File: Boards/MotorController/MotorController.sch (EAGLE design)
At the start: 16 parts, among them IC1 MC33926

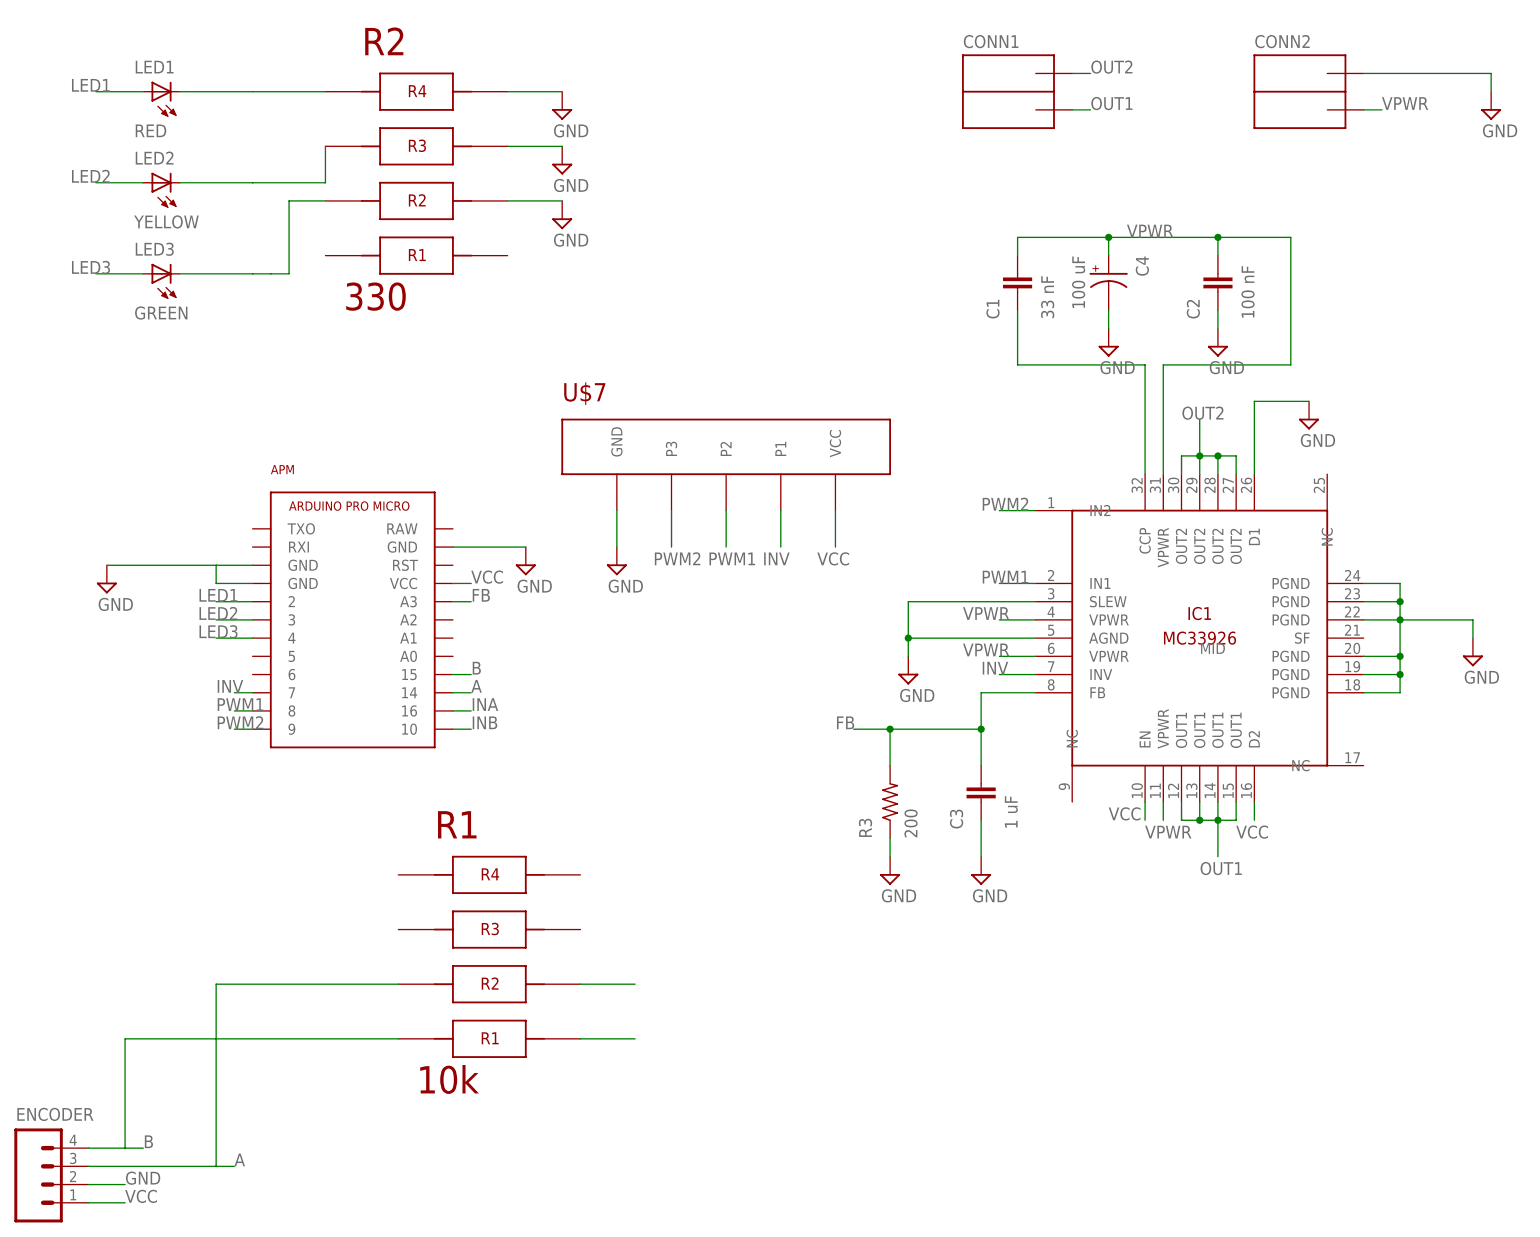
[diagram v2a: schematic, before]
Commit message: Fixed routing to arduino pins
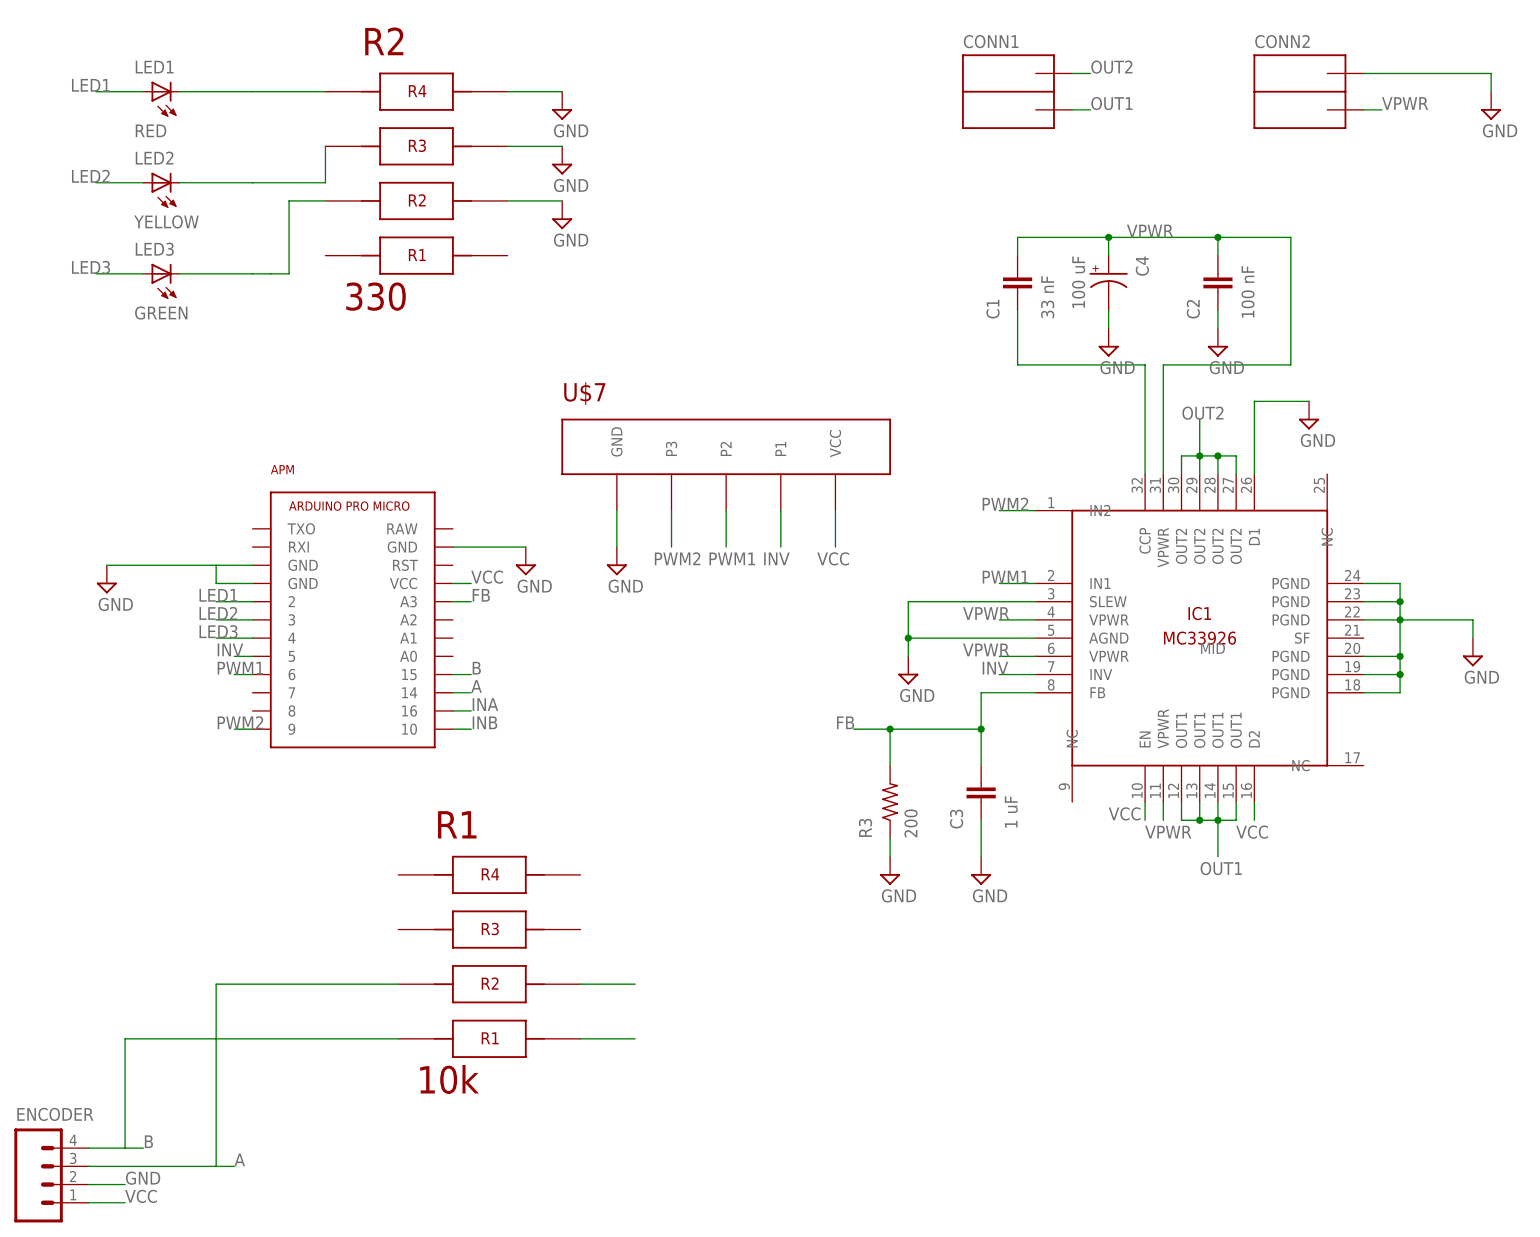
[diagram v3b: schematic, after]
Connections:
- net INV: now also APM.5; no longer APM.7
- net PWM1: now also APM.6; no longer APM.8
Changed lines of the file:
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@@
 <?xml version="1.0" encoding="utf-8"?>
 <!DOCTYPE eagle SYSTEM "eagle.dtd">
-<eagle version="9.1.3">
+<eagle version="9.2.0">
 <drawing>
 <settings>
@@
 </plain>
 <instances>
-<instance part="APM" gate="APM" x="60.96" y="93.98"/>
+<instance part="APM" gate="APM" x="60.96" y="93.98">
+<attribute name="NAME" x="50.8" y="114.3" size="1.27" layer="94"/>
+</instance>
 <instance part="FRAME1" gate="G$1" x="0" y="0">
 <attribute name="AUTHOR" x="0" y="0" size="1.778" layer="96" display="off"/>
 </instance>
 <instance part="FRAME1" gate="G$2" x="147.32" y="0">
-<attribute name="REVISION" x="147.32" y="0" size="1.778" layer="96"/>
-</instance>
-<instance part="SUPPLY2" gate="GND" x="27.94" y="99.06"/>
-<instance part="SUPPLY3" gate="GND" x="86.36" y="101.6"/>
-<instance part="LED1" gate="G$1" x="35.56" y="167.64"/>
-<instance part="SUPPLY4" gate="GND" x="91.44" y="165.1"/>
-<instance part="LED2" gate="G$1" x="35.56" y="154.94"/>
-<instance part="SUPPLY5" gate="GND" x="91.44" y="157.48"/>
-<instance part="LED3" gate="G$1" x="35.56" y="142.24"/>
-<instance part="SUPPLY6" gate="GND" x="91.44" y="149.86"/>
-<instance part="ENCODER" gate="G$1" x="17.78" y="17.78"/>
-<instance part="R1" gate="G$1" x="81.28" y="33.02"/>
-<instance part="R2" gate="G$1" x="71.12" y="142.24"/>
-<instance part="IC1" gate="G$1" x="180.34" y="91.44"/>
-<instance part="SUPPLY1" gate="GND" x="218.44" y="88.9"/>
-<instance part="SUPPLY7" gate="GND" x="195.58" y="121.92"/>
-<instance part="SUPPLY8" gate="GND" x="139.7" y="86.36"/>
-<instance part="C1" gate="G$1" x="154.94" y="139.7" rot="R90"/>
-<instance part="C2" gate="G$1" x="182.88" y="139.7" rot="R90"/>
-<instance part="C3" gate="G$1" x="149.86" y="68.58" rot="R90"/>
-<instance part="SUPPLY9" gate="GND" x="182.88" y="132.08"/>
-<instance part="SUPPLY10" gate="GND" x="167.64" y="132.08"/>
-<instance part="SUPPLY11" gate="GND" x="149.86" y="58.42"/>
-<instance part="SUPPLY12" gate="GND" x="137.16" y="58.42"/>
-<instance part="C4" gate="G$1" x="167.64" y="142.24" rot="R270"/>
-<instance part="R3" gate="G$1" x="137.16" y="68.58" rot="R90"/>
-<instance part="CONN1" gate="G$1" x="154.94" y="167.64"/>
-<instance part="CONN2" gate="G$1" x="195.58" y="167.64"/>
-<instance part="SUPPLY14" gate="GND" x="220.98" y="165.1"/>
-<instance part="U$7" gate="G$1" x="91.44" y="114.3"/>
-<instance part="SUPPLY13" gate="GND" x="99.06" y="101.6"/>
+<attribute name="LAST_DATE_TIME" x="160.02" y="1.27" size="2.54" layer="94" font="vector"/>
+<attribute name="SHEET" x="233.68" y="1.27" size="2.54" layer="94" font="vector"/>
+<attribute name="DRAWING_NAME" x="162.814" y="17.78" size="2.7432" layer="94" font="vector"/>
+<attribute name="AUTHOR" x="148.59" y="6.985" size="2.7432" layer="94" font="vector"/>
+<attribute name="REVISION" x="236.22" y="6.985" size="2.7432" layer="94" font="vector"/>
+</instance>
+<instance part="SUPPLY2" gate="GND" x="27.94" y="99.06">
+<attribute name="VALUE" x="26.67" y="95.25" size="1.778" layer="96"/>
+</instance>
+<instance part="SUPPLY3" gate="GND" x="86.36" y="101.6">
+<attribute name="VALUE" x="85.09" y="97.79" size="1.778" layer="96"/>
+</instance>
+<instance part="LED1" gate="G$1" x="35.56" y="167.64">
+<attribute name="NAME" x="31.75" y="170.18" size="1.778" layer="95"/>
+<attribute name="VALUE" x="31.75" y="161.29" size="1.778" layer="96"/>
+</instance>
+<instance part="SUPPLY4" gate="GND" x="91.44" y="165.1">
+<attribute name="VALUE" x="90.17" y="161.29" size="1.778" layer="96"/>
+</instance>
+<instance part="LED2" gate="G$1" x="35.56" y="154.94">
+<attribute name="NAME" x="31.75" y="157.48" size="1.778" layer="95"/>
+<attribute name="VALUE" x="31.75" y="148.59" size="1.778" layer="96"/>
+</instance>
+<instance part="SUPPLY5" gate="GND" x="91.44" y="157.48">
+<attribute name="VALUE" x="90.17" y="153.67" size="1.778" layer="96"/>
+</instance>
+<instance part="LED3" gate="G$1" x="35.56" y="142.24">
+<attribute name="NAME" x="31.75" y="144.78" size="1.778" layer="95"/>
+<attribute name="VALUE" x="31.75" y="135.89" size="1.778" layer="96"/>
+</instance>
+<instance part="SUPPLY6" gate="GND" x="91.44" y="149.86">
+<attribute name="VALUE" x="90.17" y="146.05" size="1.778" layer="96"/>
+</instance>
+<instance part="ENCODER" gate="G$1" x="17.78" y="17.78">
+<attribute name="VALUE" x="15.24" y="7.62" size="1.778" layer="96"/>
+<attribute name="NAME" x="15.24" y="24.13" size="1.778" layer="95"/>
+</instance>
+<instance part="R1" gate="G$1" x="81.28" y="33.02">
+<attribute name="NAME" x="73.66" y="63.5" size="3.81" layer="94" font="vector"/>
+<attribute name="VALUE" x="71.12" y="27.94" size="3.81" layer="94" font="vector"/>
+</instance>
+<instance part="R2" gate="G$1" x="71.12" y="142.24">
+<attribute name="NAME" x="63.5" y="172.72" size="3.81" layer="94" font="vector"/>
+<attribute name="VALUE" x="60.96" y="137.16" size="3.81" layer="94" font="vector"/>
+</instance>
+<instance part="IC1" gate="G$1" x="180.34" y="91.44">
+<attribute name="NAME" x="180.34" y="93.98" size="1.778" layer="94" align="bottom-center"/>
+</instance>
+<instance part="SUPPLY1" gate="GND" x="218.44" y="88.9">
+<attribute name="VALUE" x="217.17" y="85.09" size="1.778" layer="96"/>
+</instance>
+<instance part="SUPPLY7" gate="GND" x="195.58" y="121.92">
+<attribute name="VALUE" x="194.31" y="118.11" size="1.778" layer="96"/>
+</instance>
+<instance part="SUPPLY8" gate="GND" x="139.7" y="86.36">
+<attribute name="VALUE" x="138.43" y="82.55" size="1.778" layer="96"/>
+</instance>
+<instance part="C1" gate="G$1" x="154.94" y="139.7" rot="R90">
+<attribute name="NAME" x="152.4" y="135.89" size="1.778" layer="95" rot="R90"/>
+<attribute name="VALUE" x="160.02" y="135.89" size="1.778" layer="96" rot="R90"/>
+</instance>
+<instance part="C2" gate="G$1" x="182.88" y="139.7" rot="R90">
+<attribute name="NAME" x="180.34" y="135.89" size="1.778" layer="95" rot="R90"/>
+<attribute name="VALUE" x="187.96" y="135.89" size="1.778" layer="96" rot="R90"/>
+</instance>
+<instance part="C3" gate="G$1" x="149.86" y="68.58" rot="R90">
+<attribute name="NAME" x="147.32" y="64.77" size="1.778" layer="95" rot="R90"/>
+<attribute name="VALUE" x="154.94" y="64.77" size="1.778" layer="96" rot="R90"/>
+</instance>
+<instance part="SUPPLY9" gate="GND" x="182.88" y="132.08">
+<attribute name="VALUE" x="181.61" y="128.27" size="1.778" layer="96"/>
+</instance>
+<instance part="SUPPLY10" gate="GND" x="167.64" y="132.08">
+<attribute name="VALUE" x="166.37" y="128.27" size="1.778" layer="96"/>
+</instance>
+<instance part="SUPPLY11" gate="GND" x="149.86" y="58.42">
+<attribute name="VALUE" x="148.59" y="54.61" size="1.778" layer="96"/>
+</instance>
+<instance part="SUPPLY12" gate="GND" x="137.16" y="58.42">
+<attribute name="VALUE" x="135.89" y="54.61" size="1.778" layer="96"/>
+</instance>
+<instance part="C4" gate="G$1" x="167.64" y="142.24" rot="R270">
+<attribute name="NAME" x="171.45" y="144.78" size="1.778" layer="95" rot="R270"/>
+<attribute name="VALUE" x="162.56" y="144.78" size="1.778" layer="96" rot="R270"/>
+</instance>
+<instance part="R3" gate="G$1" x="137.16" y="68.58" rot="R90">
+<attribute name="NAME" x="134.62" y="63.5" size="1.778" layer="95" rot="R90"/>
+<attribute name="VALUE" x="140.97" y="63.5" size="1.778" layer="96" rot="R90"/>
+</instance>
+<instance part="CONN1" gate="G$1" x="154.94" y="167.64">
+<attribute name="NAME" x="147.32" y="173.736" size="1.778" layer="95"/>
+</instance>
+<instance part="CONN2" gate="G$1" x="195.58" y="167.64">
+<attribute name="NAME" x="187.96" y="173.736" size="1.778" layer="95"/>
+</instance>
+<instance part="SUPPLY14" gate="GND" x="220.98" y="165.1">
+<attribute name="VALUE" x="219.71" y="161.29" size="1.778" layer="96"/>
+</instance>
+<instance part="U$7" gate="G$1" x="91.44" y="114.3">
+<attribute name="NAME" x="91.44" y="124.46" size="2.54" layer="94" font="vector"/>
+</instance>
+<instance part="SUPPLY13" gate="GND" x="99.06" y="101.6">
+<attribute name="VALUE" x="97.79" y="97.79" size="1.778" layer="96"/>
+</instance>
 </instances>
 <busses>
@@
 </segment>
 <segment>
-<pinref part="APM" gate="APM" pin="7"/>
-<wire x1="48.26" y1="83.82" x2="45.72" y2="83.82" width="0.1524" layer="91"/>
-<label x="43.18" y="83.82" size="1.778" layer="95"/>
-</segment>
-<segment>
 <pinref part="U$7" gate="G$1" pin="P1"/>
 <wire x1="121.92" y1="109.22" x2="121.92" y2="104.14" width="0.1524" layer="91"/>
 <label x="119.38" y="101.6" size="1.778" layer="95"/>
 </segment>
+<segment>
+<pinref part="APM" gate="APM" pin="5"/>
+<wire x1="48.26" y1="88.9" x2="45.72" y2="88.9" width="0.1524" layer="91"/>
+<label x="43.18" y="88.9" size="1.778" layer="95"/>
+</segment>
 </net>
 <net name="PWM1" class="0">
-<segment>
-<pinref part="APM" gate="APM" pin="8"/>
-<wire x1="48.26" y1="81.28" x2="45.72" y2="81.28" width="0.1524" layer="91"/>
-<label x="43.18" y="81.28" size="1.778" layer="95"/>
-</segment>
 <segment>
 <pinref part="IC1" gate="G$1" pin="IN1"/>
@@
 <label x="111.76" y="101.6" size="1.778" layer="95"/>
 </segment>
-</net>
+<segment>
+<pinref part="APM" gate="APM" pin="6"/>
+<wire x1="48.26" y1="86.36" x2="45.72" y2="86.36" width="0.1524" layer="91"/>
+<label x="43.18" y="86.36" size="1.778" layer="95"/>
+</segment>
+</net>
